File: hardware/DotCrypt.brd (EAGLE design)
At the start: 10.2 x 20.3 mm, 7 parts, among them CN1 1X4-BIG, U1 ATMEGA328P-MU-QFN32, U3 ATSHA204-TSU

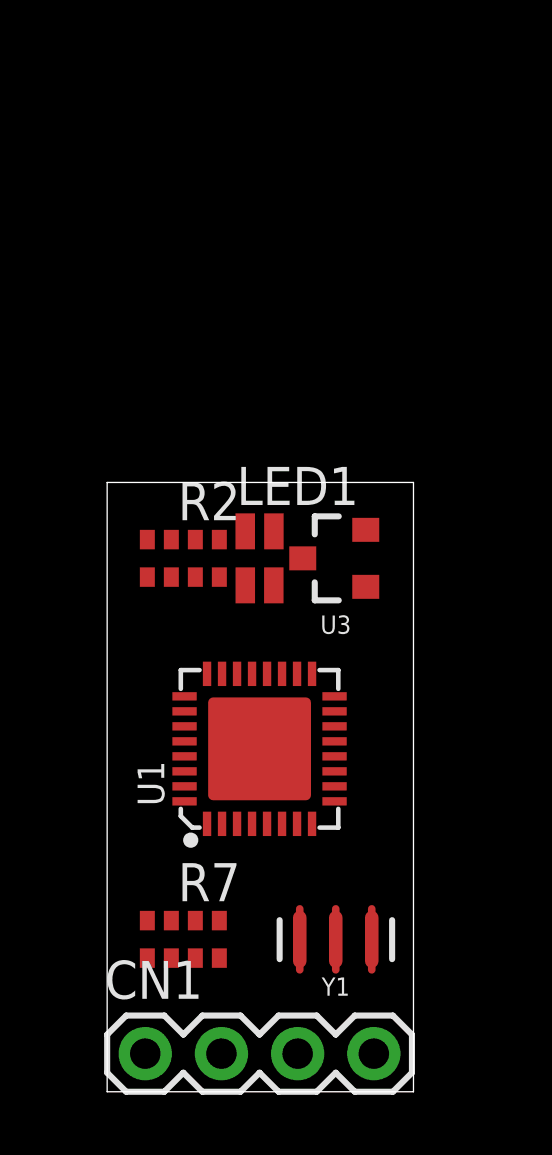
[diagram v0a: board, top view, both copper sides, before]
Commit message: Overlapping I2C & UART pins
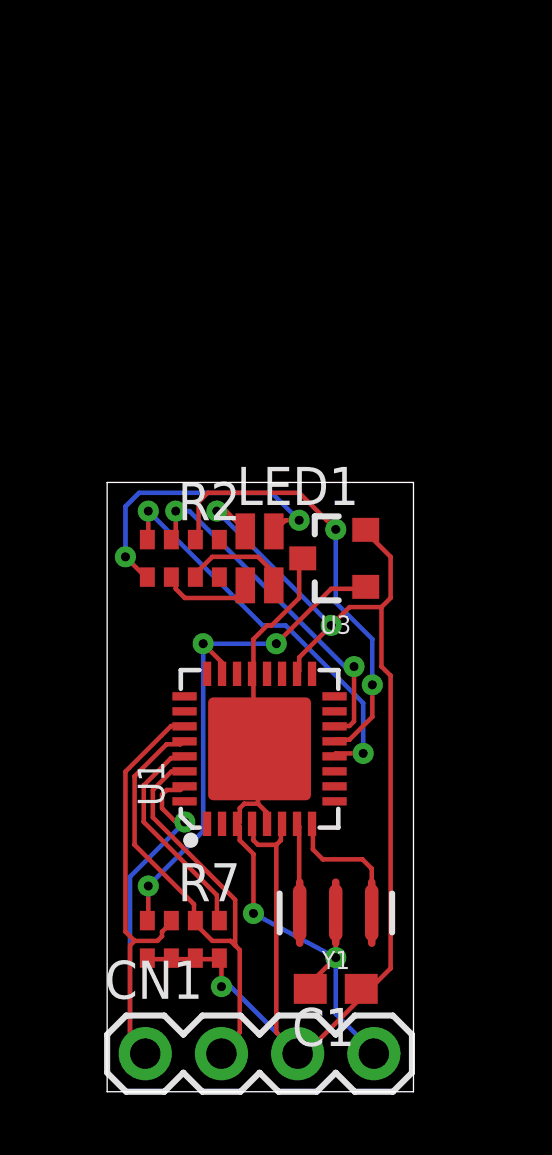
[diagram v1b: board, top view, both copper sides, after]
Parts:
- added C1: 1uF, rcl:C0603
- moved Y1 0.89 mm to (7.62, 5.97)
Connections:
- net LED renamed LED_RED
- removed net ADCENA: U1.13, U3.1
- removed net BUZZER: U1.23
- removed net OUTA: U1.14
- removed net RXD: R2.3, U1.30
- removed net TXD: R2.2, U1.31
- new net CRYPTO: R7.4, U1.23, U3.1
- new net LED_BLUE: R2.3, U1.14
- new net LED_GREEN: R2.2, U1.13
- net +3V3: now also C1.1
- net GND: now also C1.2
- net SCL: now also U1.30
- net SDA: now also U1.31
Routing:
- net +3V3: track 0.00 -> 46.7 mm, vias 0 -> 3
- net SDA: track 0.00 -> 25.0 mm, vias 0 -> 1
- net GND: track 0.00 -> 23.1 mm, vias 0 -> 2
- net SCL: track 0.00 -> 21.1 mm
- net CRYPTO: track 0.00 -> 17.5 mm, vias 0 -> 3
- net LED_GREEN: track 0.00 -> 14.9 mm, vias 0 -> 2
- net LED_RED: track 0.00 -> 13.5 mm, vias 0 -> 2
- net LED_BLUE: track 0.00 -> 11.7 mm, vias 0 -> 2
- net RED: track 0.00 -> 10.0 mm, vias 0 -> 2
- net RST: track 0.00 -> 7.30 mm
- net XTAL2: track 0.00 -> 3.66 mm
- net GREEN: track 0.00 -> 3.63 mm
- net BLUE: track 0.00 -> 3.13 mm
- net XTAL1: track 0.00 -> 2.99 mm

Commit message: Add GND planes
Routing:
- net GND: vias 2 -> 5
- added copper zone on layer 1, net GND
- added copper zone on layer 16, net GND
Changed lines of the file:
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@@
 <wire x1="6.77" y1="3.429" x2="6.77" y2="3.6204" width="0.1524" layer="1"/>
 <wire x1="6.77" y1="3.6204" x2="7.62" y2="4.4704" width="0.1524" layer="1"/>
+<polygon width="0.1524" layer="16">
+<vertex x="0" y="20.32"/>
+<vertex x="10.287" y="20.32"/>
+<vertex x="10.287" y="0"/>
+<vertex x="0" y="0"/>
+</polygon>
+<polygon width="0.1524" layer="1">
+<vertex x="0" y="0"/>
+<vertex x="10.16" y="0"/>
+<vertex x="10.16" y="20.32"/>
+<vertex x="0" y="20.32"/>
+</polygon>
+<via x="0.635" y="16.383" extent="1-16" drill="0.3"/>
+<via x="8.763" y="8.382" extent="1-16" drill="0.3"/>
+<via x="2.54" y="3.175" extent="1-16" drill="0.3"/>
 </signal>
 <signal name="SCK">

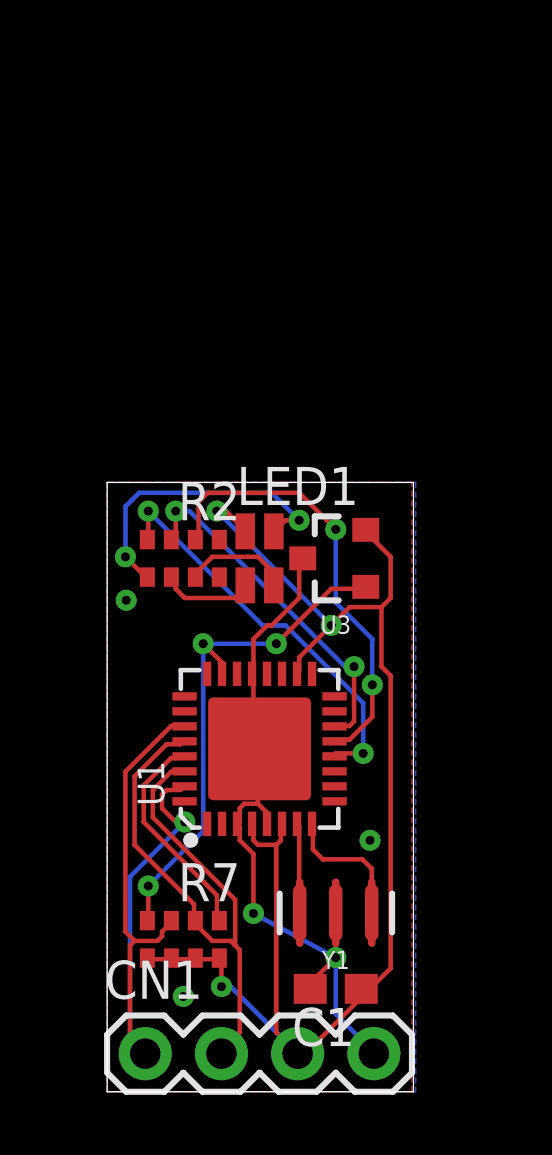
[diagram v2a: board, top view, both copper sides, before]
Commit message: Add decoupling cap, restructure connections
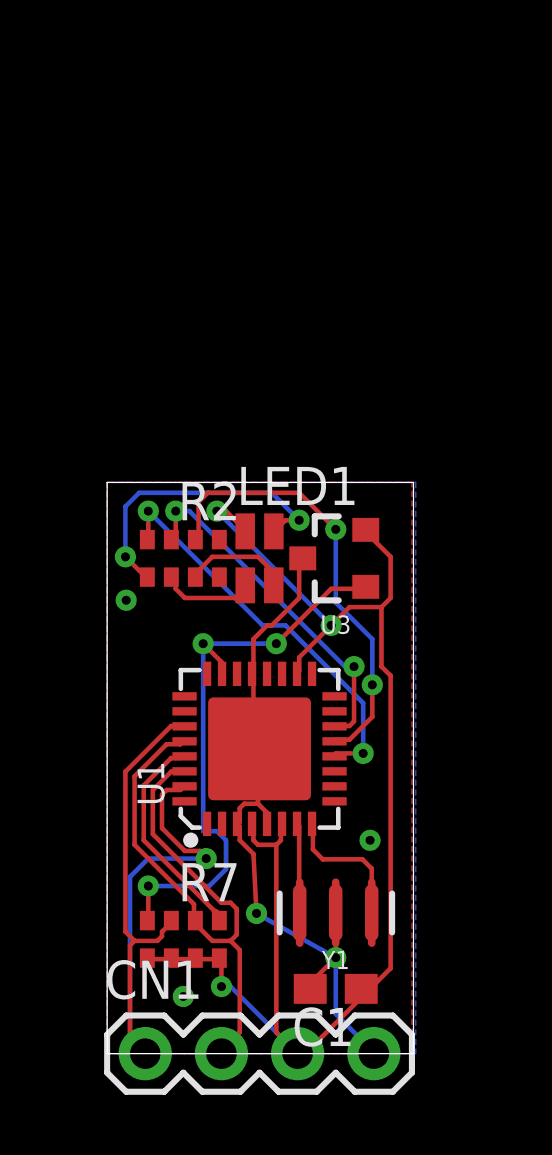
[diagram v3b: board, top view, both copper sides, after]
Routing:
- net CRYPTO: track 17.5 -> 19.5 mm
- net SDA: track 25.0 -> 26.8 mm
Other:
- board size 10.2 x 20.3 mm -> 10.2 x 19 mm
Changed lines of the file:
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@@
 <setting verticaltext="up"/>
 </settings>
-<grid distance="0.005" unitdist="inch" unit="inch" style="lines" multiple="1" display="no" altdistance="0.025" altunitdist="inch" altunit="inch"/>
+<grid distance="0.002" unitdist="inch" unit="inch" style="lines" multiple="1" display="no" altdistance="0.025" altunitdist="inch" altunit="inch"/>
 <layers>
 <layer number="1" name="Top" color="4" fill="1" visible="yes" active="yes"/>
@@
 <board>
 <plain>
-<wire x1="0" y1="0" x2="10.211" y2="0" width="0" layer="20"/>
-<wire x1="10.211" y1="0" x2="10.211" y2="20.31" width="0" layer="20"/>
+<wire x1="0" y1="1.27" x2="10.211" y2="1.27" width="0" layer="20"/>
+<wire x1="10.211" y1="1.27" x2="10.211" y2="20.31" width="0" layer="20"/>
 <wire x1="10.211" y1="20.31" x2="0" y2="20.31" width="0" layer="20"/>
-<wire x1="0" y1="20.31" x2="0" y2="0" width="0" layer="20"/>
+<wire x1="0" y1="20.31" x2="0" y2="1.27" width="0" layer="20"/>
 </plain>
 <attributes>
@@
 <wire x1="5.0292" y1="11.43" x2="5.0292" y2="9.6012" width="0.1524" layer="1"/>
 <wire x1="5.0292" y1="11.43" x2="5.08" y2="11.43" width="0.1524" layer="1"/>
-<wire x1="4.8768" y1="5.9436" x2="7.62" y2="4.4704" width="0.1524" layer="16"/>
-<wire x1="4.8768" y1="7.9248" x2="4.8768" y2="5.9436" width="0.1524" layer="1"/>
+<wire x1="4.9784" y1="5.9436" x2="7.62" y2="4.4704" width="0.1524" layer="16"/>
+<wire x1="4.8768" y1="7.9248" x2="4.9784" y2="5.9436" width="0.1524" layer="1"/>
 <wire x1="4.4196" y1="8.382" x2="4.8768" y2="7.9248" width="0.1524" layer="1"/>
 <wire x1="4.4196" y1="8.8392" x2="4.4196" y2="8.382" width="0.1524" layer="1"/>
 <wire x1="4.4196" y1="8.8392" x2="4.33" y2="8.93" width="0.1524" layer="1"/>
 <via x="7.62" y="4.4704" extent="1-16" drill="0.3"/>
-<via x="4.8768" y="5.9436" extent="1-16" drill="0.3"/>
+<via x="4.9784" y="5.9436" extent="1-16" drill="0.3"/>
 <contactref element="C1" pad="2"/>
 <wire x1="6.77" y1="3.429" x2="6.77" y2="3.6204" width="0.1524" layer="1"/>
@@
 <vertex x="0" y="20.32"/>
 <vertex x="10.287" y="20.32"/>
-<vertex x="10.287" y="0"/>
-<vertex x="0" y="0"/>
+<vertex x="10.287" y="1.27"/>
+<vertex x="0" y="1.27"/>
 </polygon>
 <polygon width="0.1524" layer="1">
-<vertex x="0" y="0"/>
-<vertex x="10.16" y="0"/>
+<vertex x="0" y="1.27"/>
+<vertex x="10.16" y="1.27"/>
 <vertex x="10.16" y="20.32"/>
 <vertex x="0" y="20.32"/>
@@
 <wire x1="1.9812" y1="10.0584" x2="2.4384" y2="10.0584" width="0.1524" layer="1"/>
 <wire x1="1.8288" y1="9.906" x2="1.9812" y2="10.0584" width="0.1524" layer="1"/>
-<wire x1="1.8288" y1="9.4488" x2="1.8288" y2="9.906" width="0.1524" layer="1"/>
-<wire x1="2.286" y1="8.9916" x2="1.8288" y2="9.4488" width="0.1524" layer="1"/>
-<wire x1="2.5908" y1="8.9916" x2="2.286" y2="8.9916" width="0.1524" layer="1"/>
-<wire x1="0.762" y1="7.1628" x2="2.5908" y2="8.9916" width="0.1524" layer="16"/>
 <wire x1="0.762" y1="1.8288" x2="0.762" y2="7.1628" width="0.1524" layer="16"/>
 <wire x1="1.2192" y1="1.3716" x2="0.762" y2="1.8288" width="0.1524" layer="16"/>
@@
 <wire x1="0.9144" y1="5.0292" x2="0.6096" y2="5.334" width="0.1524" layer="1"/>
 <wire x1="2.4384" y1="12.192" x2="2.58" y2="12.18" width="0.1524" layer="1"/>
-<via x="2.5908" y="8.9916" extent="1-16" drill="0.3"/>
+<wire x1="1.8288" y1="9.906" x2="1.8288" y2="8.7884" width="0.1524" layer="1"/>
+<wire x1="1.8288" y1="8.7884" x2="2.5908" y2="8.0264" width="0.1524" layer="1"/>
+<wire x1="2.5908" y1="8.0264" x2="3.0988" y2="8.0264" width="0.1524" layer="1"/>
+<wire x1="3.0988" y1="8.0264" x2="3.302" y2="7.7724" width="0.1524" layer="1"/>
+<via x="3.302" y="7.7724" extent="1-16" drill="0.3"/>
+<wire x1="3.302" y1="7.7724" x2="1.3716" y2="7.7724" width="0.1524" layer="16"/>
+<wire x1="1.3716" y1="7.7724" x2="0.762" y2="7.1628" width="0.1524" layer="16"/>
 </signal>
 <signal name="SCL">
@@
 <wire x1="3.5052" y1="5.0292" x2="3.048" y2="5.4864" width="0.1524" layer="1"/>
 <wire x1="4.1148" y1="5.0292" x2="3.5052" y2="5.0292" width="0.1524" layer="1"/>
-<wire x1="4.4196" y1="4.7244" x2="4.2672" y2="4.8768" width="0.1524" layer="1"/>
-<wire x1="4.2672" y1="4.8768" x2="4.1148" y2="5.0292" width="0.1524" layer="1"/>
+<wire x1="4.4196" y1="4.7244" x2="4.1148" y2="5.0292" width="0.1524" layer="1"/>
 <wire x1="4.4196" y1="1.9812" x2="4.4196" y2="4.7244" width="0.1524" layer="1"/>
 <wire x1="3.81" y1="1.3716" x2="4.4196" y2="1.9812" width="0.1524" layer="1"/>
@@
 <wire x1="2.1336" y1="10.668" x2="2.4384" y2="10.668" width="0.1524" layer="1"/>
 <wire x1="1.524" y1="10.0584" x2="2.1336" y2="10.668" width="0.1524" layer="1"/>
-<wire x1="1.524" y1="9.144" x2="1.524" y2="10.0584" width="0.1524" layer="1"/>
-<wire x1="4.2672" y1="6.4008" x2="1.524" y2="9.144" width="0.1524" layer="1"/>
-<wire x1="4.2672" y1="4.8768" x2="4.2672" y2="6.4008" width="0.1524" layer="1"/>
+<wire x1="1.524" y1="8.5852" x2="1.524" y2="10.0584" width="0.1524" layer="1"/>
 <wire x1="2.4384" y1="10.668" x2="2.58" y2="10.68" width="0.1524" layer="1"/>
 <wire x1="1.9812" y1="11.5824" x2="2.4384" y2="11.5824" width="0.1524" layer="1"/>
@@
 <wire x1="2.4384" y1="11.5824" x2="2.58" y2="11.68" width="0.1524" layer="1"/>
 <wire x1="2.8956" y1="5.7912" x2="2.94" y2="5.705" width="0.1524" layer="1"/>
+<wire x1="1.524" y1="8.5852" x2="3.81" y2="6.2992" width="0.1524" layer="1"/>
+<wire x1="3.81" y1="6.2992" x2="4.1148" y2="6.2992" width="0.1524" layer="1"/>
+<wire x1="4.1148" y1="6.2992" x2="4.318" y2="6.096" width="0.1524" layer="1"/>
+<wire x1="4.318" y1="6.096" x2="4.318" y2="5.2324" width="0.1524" layer="1"/>
+<wire x1="4.318" y1="5.2324" x2="4.1148" y2="5.0292" width="0.1524" layer="1"/>
 </signal>
 <signal name="RST">
 <contactref element="U1" pad="29"/>
 <contactref element="R7" pad="1"/>
-<wire x1="3.6576" y1="6.5532" x2="3.6576" y2="5.7912" width="0.1524" layer="1"/>
-<wire x1="1.2192" y1="8.9916" x2="3.6576" y2="6.5532" width="0.1524" layer="1"/>
-<wire x1="1.2192" y1="10.2108" x2="1.2192" y2="8.9916" width="0.1524" layer="1"/>
+<wire x1="1.2192" y1="10.2108" x2="1.2192" y2="8.382" width="0.1524" layer="1"/>
 <wire x1="2.1336" y1="11.1252" x2="1.2192" y2="10.2108" width="0.1524" layer="1"/>
 <wire x1="2.4384" y1="11.1252" x2="2.1336" y2="11.1252" width="0.1524" layer="1"/>
 <wire x1="3.6576" y1="5.7912" x2="3.74" y2="5.705" width="0.1524" layer="1"/>
 <wire x1="2.4384" y1="11.1252" x2="2.58" y2="11.18" width="0.1524" layer="1"/>
+<wire x1="1.2192" y1="8.382" x2="3.556" y2="6.0452" width="0.1524" layer="1"/>
+<wire x1="3.556" y1="6.0452" x2="3.6576" y2="5.9944" width="0.1524" layer="1"/>
+<wire x1="3.6576" y1="5.9944" x2="3.6576" y2="5.7874" width="0.1524" layer="1"/>
+<wire x1="3.6576" y1="5.7874" x2="3.74" y2="5.705" width="0.1524" layer="1"/>
 </signal>
 <signal name="+3V3">
@@
 <contactref element="R7" pad="4"/>
 <wire x1="1.3716" y1="6.858" x2="1.3716" y2="5.7912" width="0.1524" layer="1"/>
-<wire x1="3.2004" y1="8.6868" x2="1.3716" y2="6.858" width="0.1524" layer="16"/>
 <wire x1="3.2004" y1="14.9352" x2="3.2004" y2="8.6868" width="0.1524" layer="16"/>
 <wire x1="3.81" y1="14.3256" x2="3.2004" y2="14.9352" width="0.1524" layer="1"/>
@@
 <via x="3.2004" y="14.9352" extent="1-16" drill="0.3"/>
 <via x="5.6388" y="14.9352" extent="1-16" drill="0.3"/>
+<wire x1="1.3716" y1="6.858" x2="3.4036" y2="6.858" width="0.1524" layer="16"/>
+<wire x1="3.4036" y1="6.858" x2="3.9624" y2="7.4168" width="0.1524" layer="16"/>
+<wire x1="3.2004" y1="8.6868" x2="3.6576" y2="8.6868" width="0.1524" layer="16"/>
+<wire x1="3.6576" y1="8.6868" x2="3.9624" y2="8.382" width="0.1524" layer="16"/>
+<wire x1="3.9624" y1="8.382" x2="3.9624" y2="7.4168" width="0.1524" layer="16"/>
 </signal>
 <signal name="RADIO_ON">

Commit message: Add QR, sch structure lines
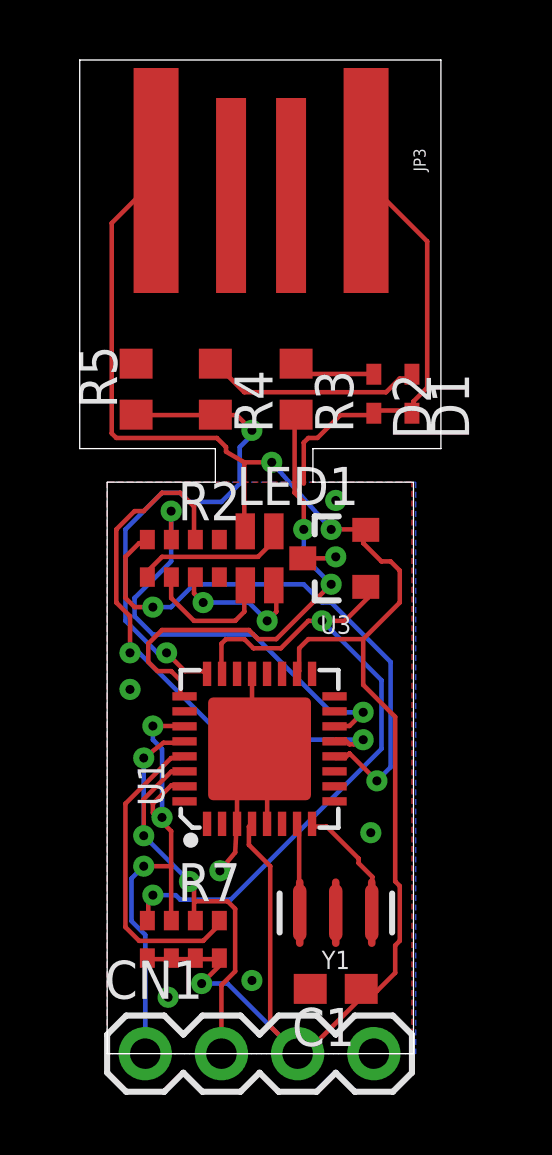
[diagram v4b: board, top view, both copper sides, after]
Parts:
- added D1, D2: MM5Z3V3, diode:SOD523
- added JP3: USBPCB, Spark:USB-A-PCB
- added R3, R4: 47Ω, rcl:R0603
- added R5: 1.5kΩ, rcl:R0603
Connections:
- new net +5V: R5.2
- new net USB_D+: D2.C, R3.1
- new net USB_D-: D1.C, R4.1
- net +3V3: now also JP3.5V; no longer U1.6
- net D+: now also R3.2
- net D-: now also R4.2, R5.1
- net GND: now also D1.A, D2.A, JP3.GND
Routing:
- net D-: track 0.00 -> 17.2 mm, vias 0 -> 2
- net D+: track 0.00 -> 15.9 mm, vias 0 -> 2
- net +3V3: track 46.7 -> 62.2 mm
- net SDA: track 26.8 -> 17.4 mm, vias 1 -> 3
- net USB_D-: track 0.00 -> 7.21 mm
- net LED_RED: track 13.5 -> 18.7 mm
- net RED: track 10.0 -> 5.14 mm, vias 2 -> 0
- net SCL: track 21.2 -> 17.1 mm, vias 0 -> 3
- net LED_GREEN: track 14.9 -> 18.8 mm
- net CRYPTO: track 19.5 -> 22.9 mm, vias 3 -> 2
- net LED_BLUE: track 11.7 -> 15.1 mm
- net RST: track 7.44 -> 10.4 mm
- net GND: track 23.0 -> 25.9 mm, vias 5 -> 7
- net USB_D+: track 0.00 -> 2.72 mm
- net BLUE: track 3.13 -> 4.46 mm
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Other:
- board size 10.2 x 19 mm -> 12 x 33.1 mm

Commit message: Add OSHW logo, vTags, rearrange USB connections
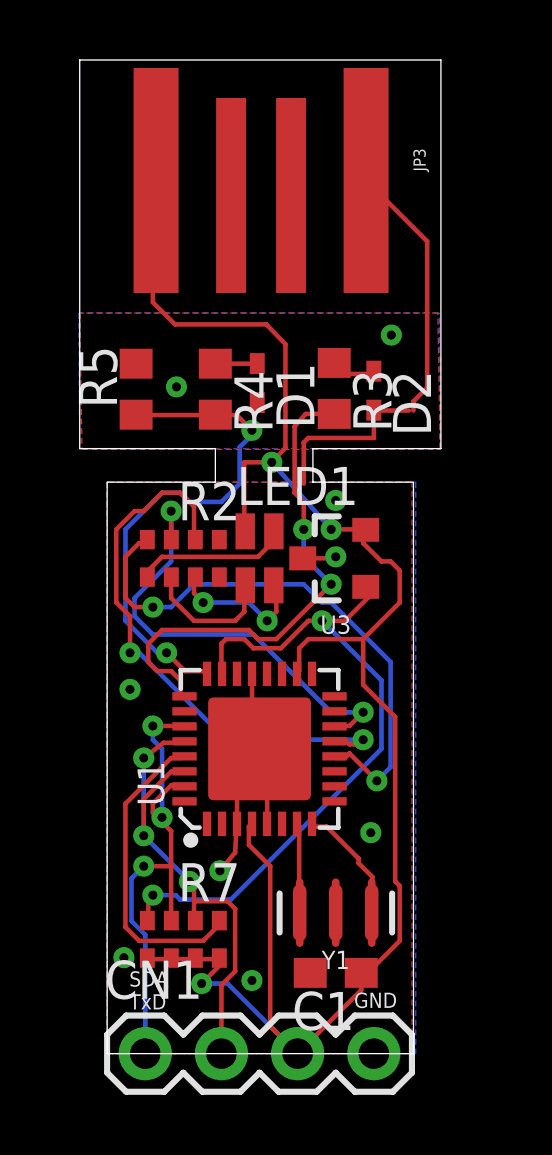
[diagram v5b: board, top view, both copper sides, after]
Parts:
- added LOGO1: OSHW-LOGOS, SparkFun-Aesthetics:OSHW-LOGO-S
- moved D1 5.17 mm to (5.00, 23.7)
- moved R3 1.27 mm to (7.57, 23.4)
- moved C1 0.53 mm to (7.62, 3.96)
- moved D2 0.10 mm to (8.89, 23.4)
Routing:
- net USB_D-: track 7.21 -> 1.40 mm
- net USB_D+: track 2.72 -> 1.54 mm
- net D+: track 15.9 -> 17.0 mm
- net GND: track 25.9 -> 26.4 mm, vias 7 -> 9
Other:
- board text added: "01/2018"
- board text added: "DotCrypt v0.1.1"
- board text added: "GND"
- board text added: "SDA TxD"
